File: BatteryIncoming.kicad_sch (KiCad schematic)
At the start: 8 parts, among them J2 DC Barrel Jack w/ Switch, K1 Relay_SPST-NO, SW1 Start, SW2 Stop, SW3 E-Stop

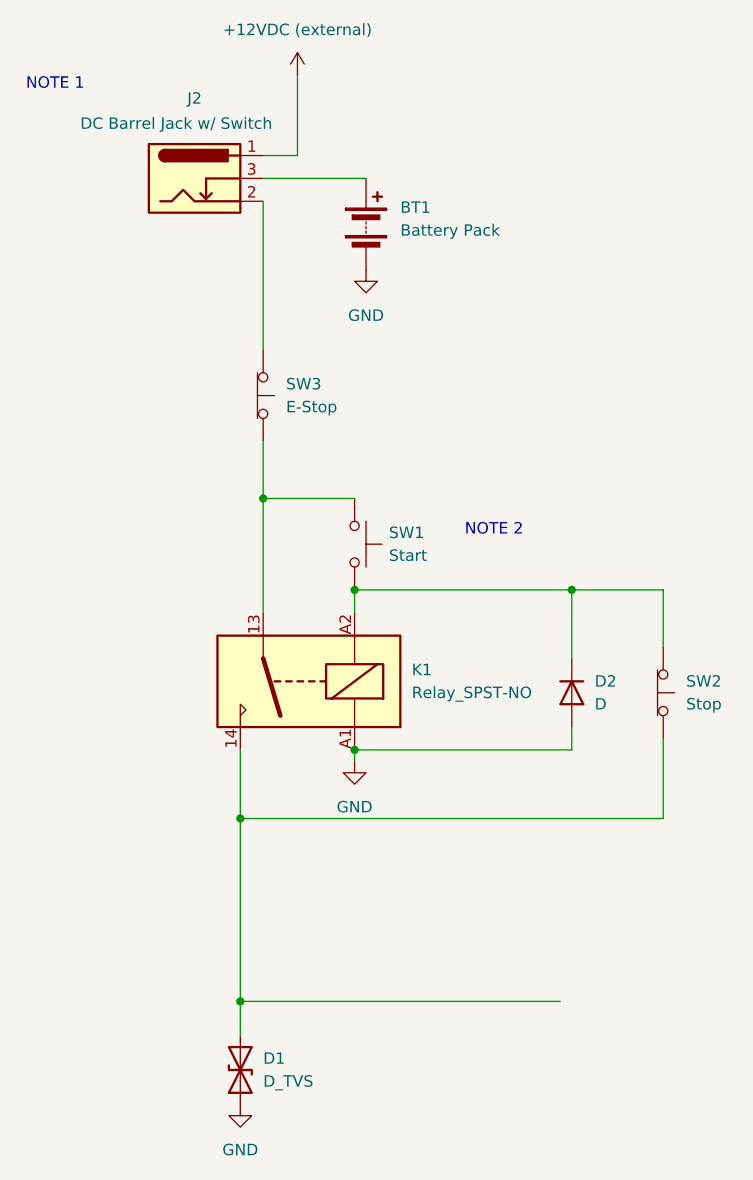
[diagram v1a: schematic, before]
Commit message: Implemented mcu/sensors/motors + modified info + modified .gitignore
- Confirmed pinouts on NUCLEO64-G474RE and routed them from dev board to
swerve drives
- Individual swerve drives (with/without TOF sensors) are Hierarchial
sheets
- .history was acting like a submodule and is not needed because we have
git so it was removed and its presence was added to .gitignore
- Added info on NC pins
- Still need confirmation on TBD pins + SPI signals
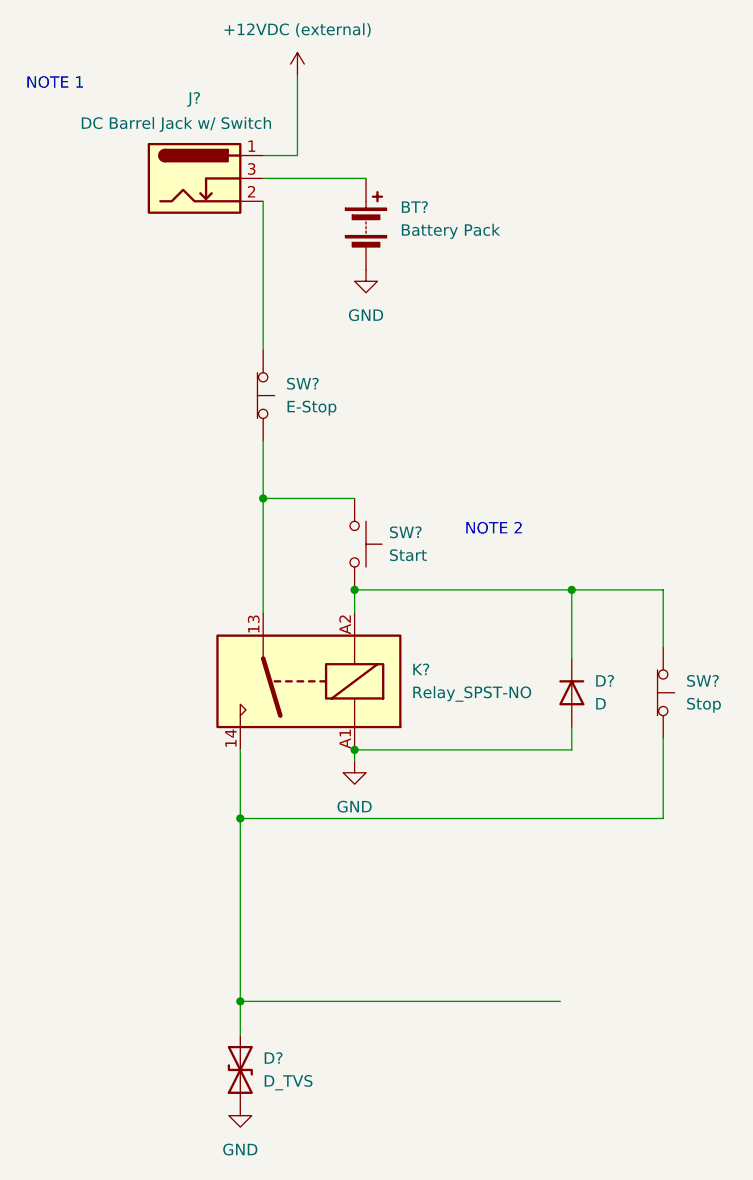
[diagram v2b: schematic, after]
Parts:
- renumbered BT1 to BT?, D2 to D?, D1 to D?, J2 to J?, K1 to K?, SW2 to SW?, SW1 to SW?, SW3 to SW?
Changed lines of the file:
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@@
 		(dnp no)
 		(fields_autoplaced yes)
-		(property "Reference" "SW2"
+		(property "Reference" "SW?"
 			(at 93.98 91.4399 90)
 			(show_name no)
@@
 			(project "PLDR_rev1"
 				(path "/044e3193-aa4e-4ad4-a125-51ae4829b9ed/21ff1059-a78f-4c64-a100-018957f7182e"
-					(reference "SW2")
+					(reference "SW?")
 					(unit 1)
 				)
@@
 		(dnp no)
 		(fields_autoplaced yes)
-		(property "Reference" "SW1"
+		(property "Reference" "SW?"
 			(at 60.96 74.9299 90)
 			(show_name no)
@@
 			(project "PLDR_rev1"
 				(path "/044e3193-aa4e-4ad4-a125-51ae4829b9ed/21ff1059-a78f-4c64-a100-018957f7182e"
-					(reference "SW1")
+					(reference "SW?")
 					(unit 1)
 				)
@@
 		(dnp no)
 		(fields_autoplaced yes)
-		(property "Reference" "D2"
+		(property "Reference" "D?"
 			(at 83.82 91.4399 90)
 			(show_name no)
@@
 			(project "PLDR_rev1"
 				(path "/044e3193-aa4e-4ad4-a125-51ae4829b9ed/21ff1059-a78f-4c64-a100-018957f7182e"
-					(reference "D2")
+					(reference "D?")
 					(unit 1)
 				)
@@
 		(dnp no)
 		(fields_autoplaced yes)
-		(property "Reference" "#PWR03"
+		(property "Reference" "#PWR?"
 			(at 57.15 106.68 0)
 			(hide yes)
@@
 			(project "PLDR_rev1"
 				(path "/044e3193-aa4e-4ad4-a125-51ae4829b9ed/21ff1059-a78f-4c64-a100-018957f7182e"
-					(reference "#PWR03")
+					(reference "#PWR?")
 					(unit 1)
 				)
@@
 		(dnp no)
 		(fields_autoplaced yes)
-		(property "Reference" "BT1"
+		(property "Reference" "BT?"
 			(at 62.23 38.7984 0)
 			(show_name no)
@@
 			(project "PLDR_rev1"
 				(path "/044e3193-aa4e-4ad4-a125-51ae4829b9ed/21ff1059-a78f-4c64-a100-018957f7182e"
-					(reference "BT1")
+					(reference "BT?")
 					(unit 1)
 				)
@@
 		(in_pos_files yes)
 		(dnp no)
-		(property "Reference" "J2"
+		(property "Reference" "J?"
 			(at 39.37 26.67 0)
 			(show_name no)
@@
 			(project "PLDR_rev1"
 				(path "/044e3193-aa4e-4ad4-a125-51ae4829b9ed/21ff1059-a78f-4c64-a100-018957f7182e"
-					(reference "J2")
+					(reference "J?")
 					(unit 1)
 				)
@@
 		(dnp no)
 		(fields_autoplaced yes)
-		(property "Reference" "K1"
+		(property "Reference" "K?"
 			(at 63.5 90.1699 0)
 			(show_name no)
@@
 			(project "PLDR_rev1"
 				(path "/044e3193-aa4e-4ad4-a125-51ae4829b9ed/21ff1059-a78f-4c64-a100-018957f7182e"
-					(reference "K1")
+					(reference "K?")
 					(unit 1)
 				)
@@
 		(dnp no)
 		(fields_autoplaced yes)
-		(property "Reference" "#PWR01"
+		(property "Reference" "#PWR?"
 			(at 50.8 27.94 0)
 			(hide yes)
@@
 			(project "PLDR_rev1"
 				(path "/044e3193-aa4e-4ad4-a125-51ae4829b9ed/21ff1059-a78f-4c64-a100-018957f7182e"
-					(reference "#PWR01")
+					(reference "#PWR?")
 					(unit 1)
 				)
@@
 		(dnp no)
 		(fields_autoplaced yes)
-		(property "Reference" "D1"
+		(property "Reference" "D?"
 			(at 46.99 133.3499 90)
 			(show_name no)
@@
 			(project "PLDR_rev1"
 				(path "/044e3193-aa4e-4ad4-a125-51ae4829b9ed/21ff1059-a78f-4c64-a100-018957f7182e"
-					(reference "D1")
+					(reference "D?")
 					(unit 1)
 				)
@@
 		(dnp no)
 		(fields_autoplaced yes)
-		(property "Reference" "SW3"
+		(property "Reference" "SW?"
 			(at 49.53 58.4199 90)
 			(show_name no)
@@
 			(project "PLDR_rev1"
 				(path "/044e3193-aa4e-4ad4-a125-51ae4829b9ed/21ff1059-a78f-4c64-a100-018957f7182e"
-					(reference "SW3")
+					(reference "SW?")
 					(unit 1)
 				)
@@
 		(dnp no)
 		(fields_autoplaced yes)
-		(property "Reference" "#PWR04"
+		(property "Reference" "#PWR?"
 			(at 44.45 144.78 0)
 			(hide yes)
@@
 			(project "PLDR_rev1"
 				(path "/044e3193-aa4e-4ad4-a125-51ae4829b9ed/21ff1059-a78f-4c64-a100-018957f7182e"
-					(reference "#PWR04")
+					(reference "#PWR?")
 					(unit 1)
 				)
@@
 		(dnp no)
 		(fields_autoplaced yes)
-		(property "Reference" "#PWR02"
+		(property "Reference" "#PWR?"
 			(at 58.42 52.07 0)
 			(hide yes)
@@
 			(project "PLDR_rev1"
 				(path "/044e3193-aa4e-4ad4-a125-51ae4829b9ed/21ff1059-a78f-4c64-a100-018957f7182e"
-					(reference "#PWR02")
-					(unit 1)
-				)
+					(reference "#PWR?")
+					(unit 1)
+				)
